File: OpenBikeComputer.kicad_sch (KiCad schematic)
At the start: 0 parts

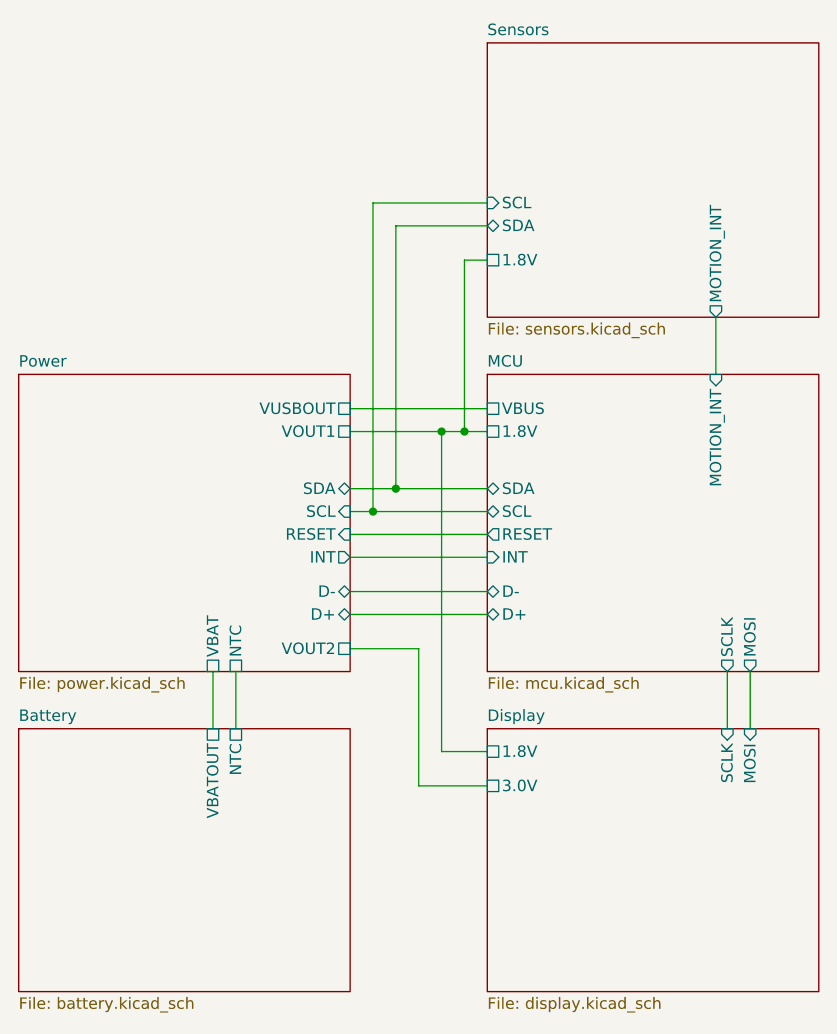
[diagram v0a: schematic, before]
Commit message: use separate i2c bus for PMIC
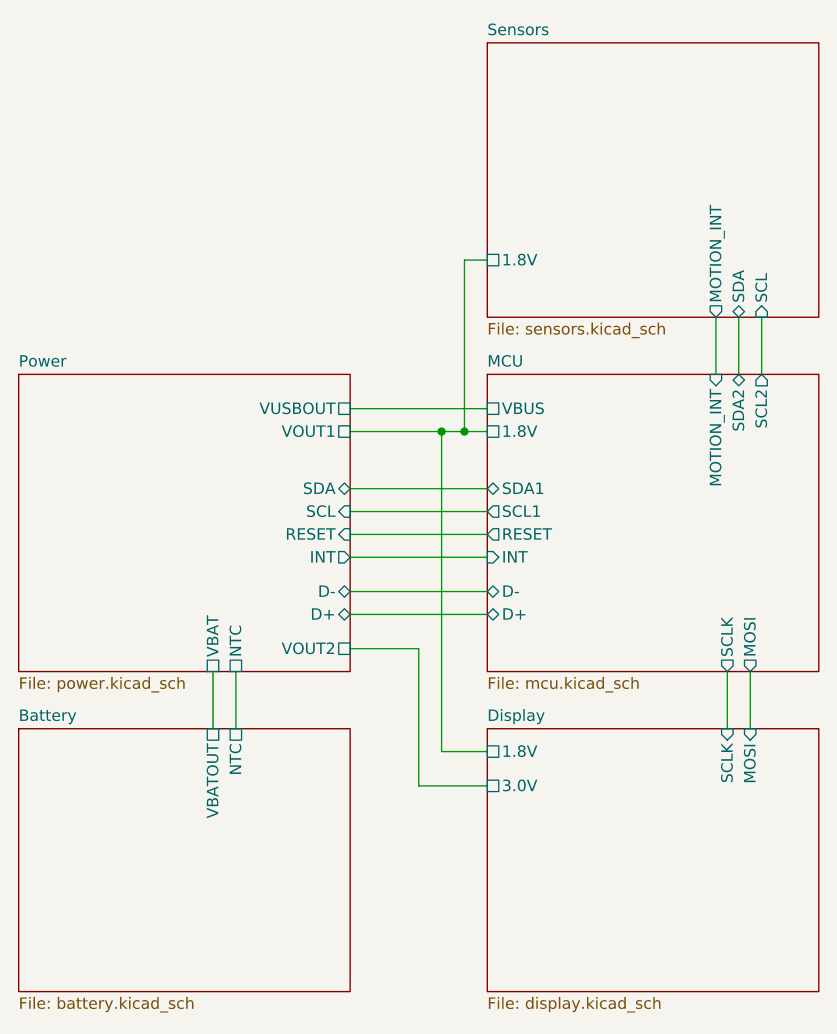
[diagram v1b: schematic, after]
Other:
- sheet MCU ports: added SCL1, SCL2, SDA1, SDA2; removed SCL, SDA
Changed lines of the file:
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@@
 		(color 0 0 0 0)
 	)
-	(junction
-		(at 101.6 72.39)
-		(diameter 0)
-		(color 0 0 0 0)
-	)
-	(junction
-		(at 99.06 74.93)
-		(diameter 0)
-		(color 0 0 0 0)
-	)
 	(wire
 		(pts
@@
 	(wire
 		(pts
-			(xy 111.76 40.64) (xy 99.06 40.64)
-		)
-		(stroke
-			(width 0)
-			(type default)
-		)
-	)
-	(wire
-		(pts
 			(xy 109.22 66.04) (xy 111.76 66.04)
 		)
@@
 	(wire
 		(pts
-			(xy 99.06 74.93) (xy 111.76 74.93)
-		)
-		(stroke
-			(width 0)
-			(type default)
-		)
-	)
-	(wire
-		(pts
-			(xy 99.06 40.64) (xy 99.06 74.93)
+			(xy 96.52 74.93) (xy 111.76 74.93)
 		)
 		(stroke
@@
 	(wire
 		(pts
-			(xy 101.6 72.39) (xy 111.76 72.39)
-		)
-		(stroke
-			(width 0)
-			(type default)
-		)
-	)
-	(wire
-		(pts
-			(xy 101.6 43.18) (xy 101.6 72.39)
-		)
-		(stroke
-			(width 0)
-			(type default)
-		)
-	)
-	(wire
-		(pts
-			(xy 96.52 74.93) (xy 99.06 74.93)
-		)
-		(stroke
-			(width 0)
-			(type default)
-		)
-	)
-	(wire
-		(pts
-			(xy 111.76 43.18) (xy 101.6 43.18)
+			(xy 96.52 72.39) (xy 111.76 72.39)
+		)
+		(stroke
+			(width 0)
+			(type default)
+		)
+	)
+	(wire
+		(pts
+			(xy 139.7 53.34) (xy 139.7 59.69)
+		)
+		(stroke
+			(width 0)
+			(type default)
+		)
+	)
+	(wire
+		(pts
+			(xy 142.24 53.34) (xy 142.24 59.69)
 		)
 		(stroke
@@
 		(pts
 			(xy 109.22 66.04) (xy 109.22 46.99)
-		)
-		(stroke
-			(width 0)
-			(type default)
-		)
-	)
-	(wire
-		(pts
-			(xy 96.52 72.39) (xy 101.6 72.39)
 		)
 		(stroke
@@
 		)
 		(pin "SDA" bidirectional
-			(at 111.76 43.18 180)
+			(at 139.7 53.34 270)
 			(effects
 				(font
@@
 		)
 		(pin "SCL" input
-			(at 111.76 40.64 180)
+			(at 142.24 53.34 270)
 			(effects
 				(font
@@
 			)
 		)
-		(pin "SDA" bidirectional
-			(at 111.76 72.39 180)
-			(effects
-				(font
-					(size 1.27 1.27)
-				)
-				(justify left)
-			)
-		)
-		(pin "SCL" bidirectional
-			(at 111.76 74.93 180)
-			(effects
-				(font
-					(size 1.27 1.27)
-				)
-				(justify left)
-			)
-		)
 		(pin "MOTION_INT" input
 			(at 137.16 59.69 90)
 			(effects
 				(font
+					(size 1.27 1.27)
+				)
+				(justify right)
+			)
+		)
+		(pin "SCL1" output
+			(at 111.76 74.93 180)
+			(effects
+				(font
+					(size 1.27 1.27)
+				)
+				(justify left)
+			)
+		)
+		(pin "SDA1" bidirectional
+			(at 111.76 72.39 180)
+			(effects
+				(font
+					(size 1.27 1.27)
+				)
+				(justify left)
+			)
+		)
+		(pin "SCL2" output
+			(at 142.24 59.69 90)
+			(effects
+				(font
+					(size 1.27 1.27)
+				)
+				(justify right)
+			)
+		)
+		(pin "SDA2" bidirectional
+			(at 139.7 59.69 90)
+			(effects
+				(font

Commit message: switch out SoC, stuff is in the air
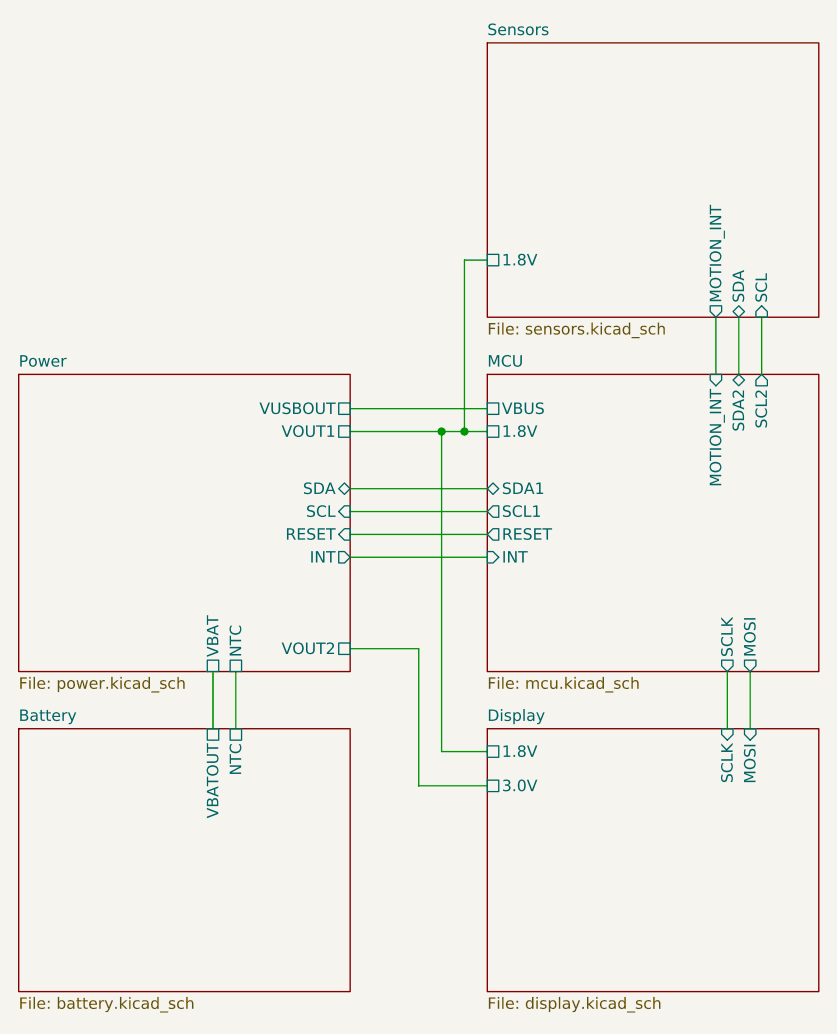
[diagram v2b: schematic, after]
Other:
- sheet MCU ports: added none; removed D+, D-
- sheet Power ports: added none; removed D+, D-
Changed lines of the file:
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@@
-	(wire
-		(pts
-			(xy 96.52 86.36) (xy 111.76 86.36)
-		)
-		(stroke
-			(width 0)
-			(type default)
-		)
-	)
 	(wire
 		(pts
@@
 		(pts
 			(xy 142.24 53.34) (xy 142.24 59.69)
-		)
-		(stroke
-			(width 0)
-			(type default)
-		)
-	)
-	(wire
-		(pts
-			(xy 96.52 83.82) (xy 111.76 83.82)
 		)
 		(stroke
@@
 			)
 		)
-		(pin "D+" bidirectional
-			(at 96.52 86.36 0)
-			(effects
-				(font
-					(size 1.27 1.27)
-				)
-				(justify right)
-			)
-		)
-		(pin "D-" bidirectional
-			(at 96.52 83.82 0)
-			(effects
-				(font
-					(size 1.27 1.27)
-				)
-				(justify right)
-			)
-		)
 		(pin "INT" output
 			(at 96.52 80.01 0)
@@
 			)
 		)
-		(pin "D-" bidirectional
-			(at 111.76 83.82 180)
-			(effects
-				(font
-					(size 1.27 1.27)
-				)
-				(justify left)
-			)
-		)
-		(pin "D+" bidirectional
-			(at 111.76 86.36 180)
-			(effects
-				(font
-					(size 1.27 1.27)
-				)
-				(justify left)
-			)
-		)

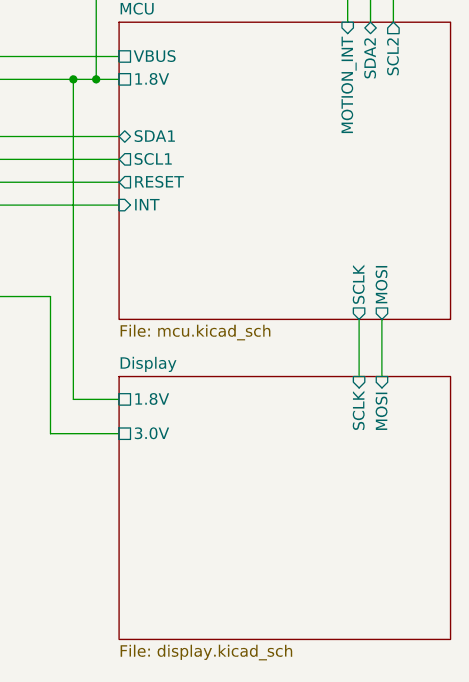
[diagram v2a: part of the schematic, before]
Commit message: finish oled driver circuit
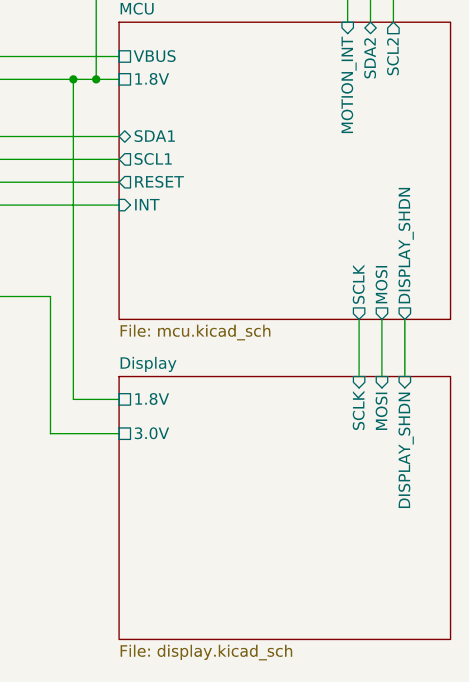
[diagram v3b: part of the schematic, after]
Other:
- sheet Display ports: added DISPLAY_SHDN; removed none
- sheet MCU ports: added DISPLAY_SHDN; removed none
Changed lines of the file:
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@@
+	(wire
+		(pts
+			(xy 143.51 92.71) (xy 143.51 99.06)
+		)
+		(stroke
+			(width 0)
+			(type default)
+		)
+	)
 	(wire
 		(pts
@@
 			)
 		)
+		(pin "DISPLAY_SHDN" input
+			(at 143.51 99.06 90)
+			(effects
+				(font
+					(size 1.27 1.27)
+				)
+				(justify right)
+			)
+		)
 		(instances
 			(project "OpenBikeComputer"
@@
 			)
 		)
+		(pin "DISPLAY_SHDN" output
+			(at 143.51 92.71 270)
+			(effects
+				(font
+					(size 1.27 1.27)
+				)
+				(justify left)
+			)
+		)

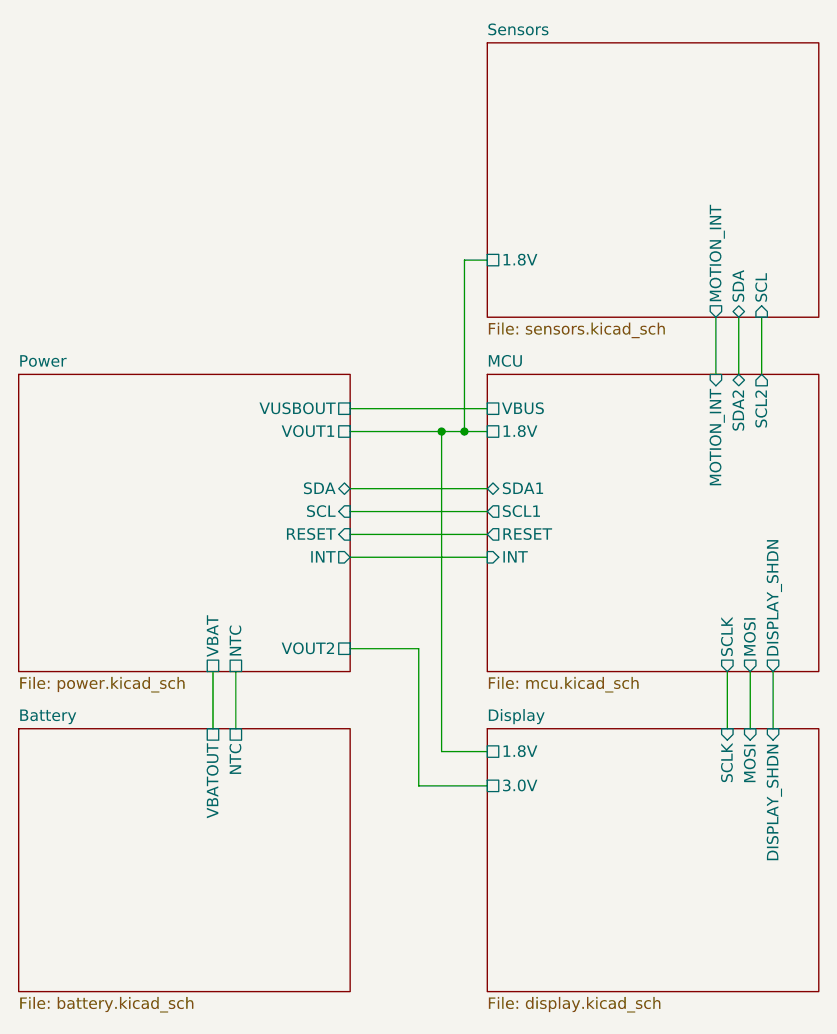
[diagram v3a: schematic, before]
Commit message: rfinish routing PMIC (pretty crap routing)
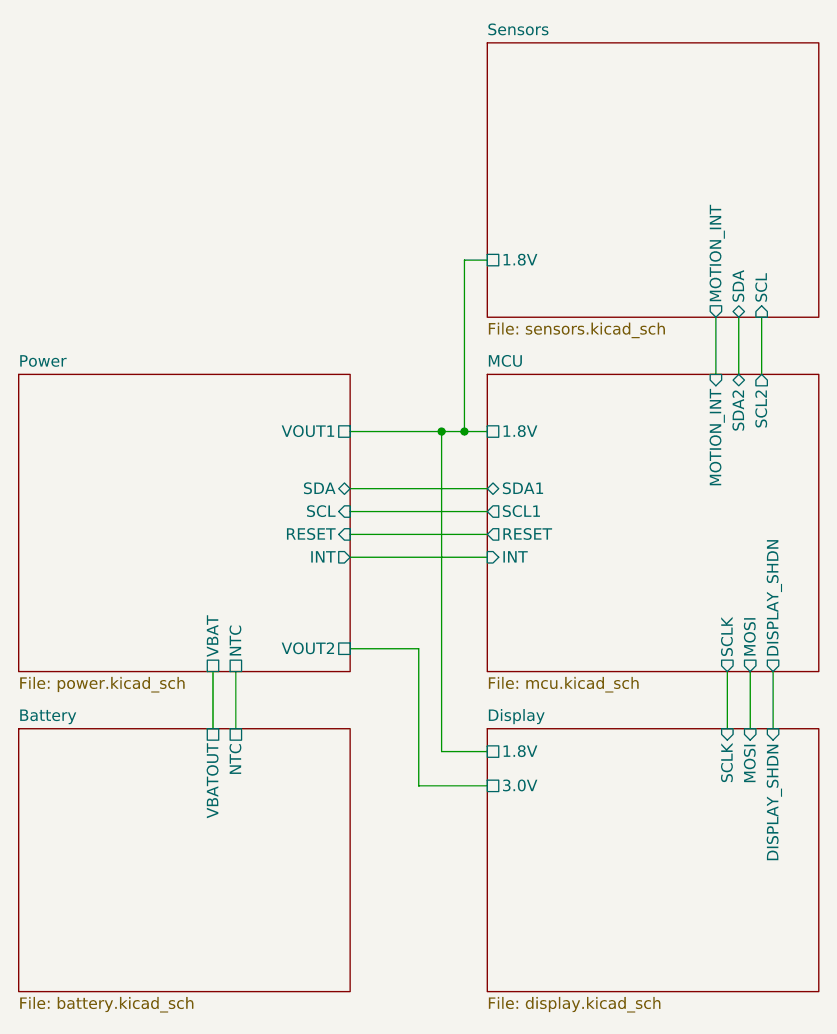
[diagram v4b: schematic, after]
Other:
- sheet MCU ports: added none; removed VBUS
- sheet Power ports: added none; removed VUSBOUT
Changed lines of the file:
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@@
-	(wire
-		(pts
-			(xy 96.52 63.5) (xy 111.76 63.5)
-		)
-		(stroke
-			(width 0)
-			(type default)
-		)
-	)
 	(wire
 		(pts
@@
 			)
 		)
-		(pin "VUSBOUT" passive
-			(at 96.52 63.5 0)
-			(effects
-				(font
-					(size 1.27 1.27)
-				)
-				(justify right)
-			)
-		)
 		(instances
 			(project "OpenBikeComputer"
@@
 			)
 		)
-		(pin "VBUS" passive
-			(at 111.76 63.5 180)
-			(effects
-				(font
-					(size 1.27 1.27)
-				)
-				(justify left)
-			)
-		)

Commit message: route PMIC
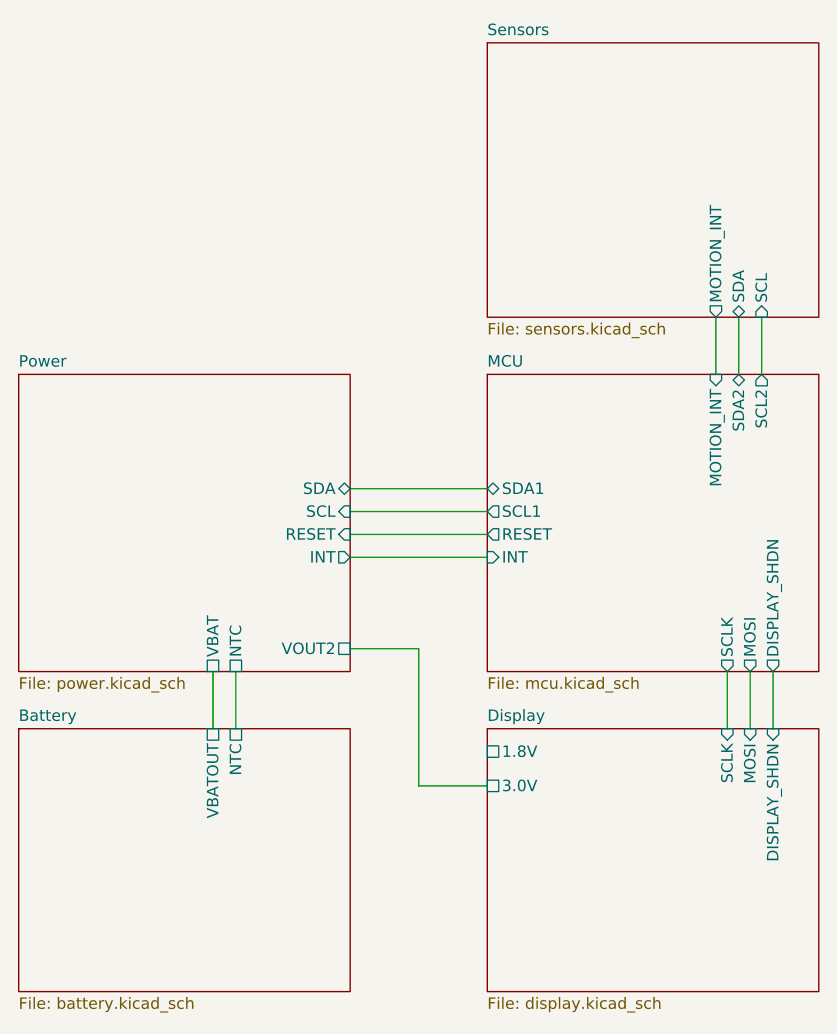
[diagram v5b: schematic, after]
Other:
- sheet MCU ports: added none; removed 1.8V
- sheet Power ports: added none; removed VOUT1
- sheet Sensors ports: added none; removed 1.8V
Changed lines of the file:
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@@
 	(generator_version "8.0")
 	(paper "A4")
-	(junction
-		(at 106.68 66.04)
-		(diameter 0)
-		(color 0 0 0 0)
-	)
-	(junction
-		(at 109.22 66.04)
-		(diameter 0)
-		(color 0 0 0 0)
-	)
-	(wire
-		(pts
-			(xy 106.68 101.6) (xy 106.68 66.04)
-		)
-		(stroke
-			(width 0)
-			(type default)
-		)
-	)
 	(wire
 		(pts
@@
 	(wire
 		(pts
-			(xy 109.22 46.99) (xy 111.76 46.99)
-		)
-		(stroke
-			(width 0)
-			(type default)
-		)
-	)
-	(wire
-		(pts
-			(xy 109.22 66.04) (xy 111.76 66.04)
-		)
-		(stroke
-			(width 0)
-			(type default)
-		)
-	)
-	(wire
-		(pts
 			(xy 96.52 74.93) (xy 111.76 74.93)
 		)
@@
 	(wire
 		(pts
-			(xy 96.52 66.04) (xy 106.68 66.04)
-		)
-		(stroke
-			(width 0)
-			(type default)
-		)
-	)
-	(wire
-		(pts
 			(xy 96.52 72.39) (xy 111.76 72.39)
 		)
@@
 		(pts
 			(xy 142.24 53.34) (xy 142.24 59.69)
-		)
-		(stroke
-			(width 0)
-			(type default)
-		)
-	)
-	(wire
-		(pts
-			(xy 106.68 66.04) (xy 109.22 66.04)
-		)
-		(stroke
-			(width 0)
-			(type default)
-		)
-	)
-	(wire
-		(pts
-			(xy 109.22 66.04) (xy 109.22 46.99)
-		)
-		(stroke
-			(width 0)
-			(type default)
-		)
-	)
-	(wire
-		(pts
-			(xy 111.76 101.6) (xy 106.68 101.6)
 		)
 		(stroke
@@
 			)
 		)
-		(pin "VOUT1" passive
-			(at 96.52 66.04 0)
-			(effects
-				(font
-					(size 1.27 1.27)
-				)
-				(justify right)
-			)
-		)
 		(pin "NTC" passive
 			(at 83.82 92.71 270)
@@
 			)
 		)
-		(pin "1.8V" passive
-			(at 111.76 46.99 180)
-			(effects
-				(font
-					(size 1.27 1.27)
-				)
-				(justify left)
-			)
-		)
 		(pin "MOTION_INT" output
 			(at 137.16 53.34 270)
@@
 			)
 		)
-		(pin "1.8V" passive
-			(at 111.76 66.04 180)
-			(effects
-				(font
-					(size 1.27 1.27)
-				)
-				(justify left)
-			)
-		)
